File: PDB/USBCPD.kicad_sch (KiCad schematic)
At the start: 43 parts, among them J1 USB_C_Receptacle, Q3 STL6P3LLH6, Q4 STL6P3LLH6, U6 ST1S14PHR, U7 STUSB4700YQTR, U8 STR2P3LLH6, U9 LM76005QRNPRQ1

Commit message: added sd card
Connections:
- net at C22.1, C23.1, C24.1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: now also U7.24 (VDD)
- no-connect marks 14 -> 16
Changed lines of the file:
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@@
-	)
-	(junction
-		(at 353.06 160.02)
-		(diameter 0)
-		(color 0 0 0 0)
 	)
 	(junction
@@
 	)
 	(junction
+		(at 368.3 166.37)
+		(diameter 0)
+		(color 0 0 0 0)
+	)
+	(junction
 		(at 317.5 160.02)
 		(diameter 0)
@@
 	)
 	(junction
+		(at 368.3 160.02)
+		(diameter 0)
+		(color 0 0 0 0)
+	)
+	(junction
 		(at 317.5 162.56)
 		(diameter 0)
@@
 		(diameter 0)
 		(color 0 0 0 0)
+	)
+	(no_connect
+		(at 393.7 223.52)
 	)
 	(no_connect
@@
 	)
 	(no_connect
+		(at 393.7 212.09)
+	)
+	(no_connect
 		(at 480.06 170.18)
 	)
@@
 	(wire
 		(pts
+			(xy 368.3 160.02) (xy 382.27 160.02)
+		)
+		(stroke
+			(width 0)
+			(type default)
+		)
+	)
+	(wire
+		(pts
 			(xy 480.06 218.44) (xy 480.06 219.71)
 		)
@@
 	(wire
 		(pts
-			(xy 353.06 160.02) (xy 353.06 166.37)
+			(xy 368.3 160.02) (xy 368.3 166.37)
 		)
 		(stroke
@@
 	(wire
 		(pts
+			(xy 368.3 179.07) (xy 368.3 166.37)
+		)
+		(stroke
+			(width 0)
+			(type default)
+		)
+	)
+	(wire
+		(pts
 			(xy 229.87 165.1) (xy 229.87 160.02)
 		)
@@
 	(wire
 		(pts
-			(xy 353.06 160.02) (xy 382.27 160.02)
-		)
-		(stroke
-			(width 0)
-			(type default)
-		)
-	)
-	(wire
-		(pts
 			(xy 326.39 234.95) (xy 359.41 234.95)
 		)
@@
 	(wire
 		(pts
-			(xy 330.2 160.02) (xy 353.06 160.02)
+			(xy 330.2 160.02) (xy 368.3 160.02)
 		)
 		(stroke
@@
 		)
 		(stroke
+			(width 0)
+			(type default)
+		)
+	)
+	(wire
+		(pts
+			(xy 368.3 166.37) (xy 353.06 166.37)
+		)
+		(stroke

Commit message: added fuses to each
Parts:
- added F4: TR/3216FF15-R, symbol Device:Fuse
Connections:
- net at C28.1, J1.A4 (VBUS): now also F4.2; no longer Q4.5_8, U7.18 (VBUS_SENSE)
- new net: F4.1, Q4.5_8, U7.18 (VBUS_SENSE)
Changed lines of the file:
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@@
 	)
 	(junction
-		(at 452.12 160.02)
-		(diameter 0)
-		(color 0 0 0 0)
-	)
-	(junction
 		(at 90.17 203.2)
 		(diameter 0)
@@
 	)
 	(junction
+		(at 467.36 160.02)
+		(diameter 0)
+		(color 0 0 0 0)
+	)
+	(junction
 		(at 74.93 154.94)
 		(diameter 0)
@@
 	)
 	(junction
-		(at 467.36 160.02)
-		(diameter 0)
-		(color 0 0 0 0)
-	)
-	(junction
 		(at 364.49 179.07)
 		(diameter 0)
@@
 	)
 	(junction
+		(at 452.12 160.02)
+		(diameter 0)
+		(color 0 0 0 0)
+	)
+	(junction
 		(at 90.17 193.04)
 		(diameter 0)
@@
 	(wire
 		(pts
+			(xy 463.55 160.02) (xy 467.36 160.02)
+		)
+		(stroke
+			(width 0)
+			(type default)
+		)
+	)
+	(wire
+		(pts
 			(xy 306.07 162.56) (xy 317.5 162.56)
 		)
@@
 	(wire
 		(pts
-			(xy 452.12 160.02) (xy 467.36 160.02)
-		)
-		(stroke
-			(width 0)
-			(type default)
-		)
-	)
-	(wire
-		(pts
 			(xy 427.99 180.34) (xy 427.99 194.31)
 		)
@@
 	(wire
 		(pts
+			(xy 452.12 160.02) (xy 455.93 160.02)
+		)
+		(stroke
+			(width 0)
+			(type default)
+		)
+	)
+	(wire
+		(pts
 			(xy 477.52 210.82) (xy 480.06 210.82)
 		)
@@
 					(unit 1)
 				)
+			)
+		)
+	)
+	(symbol
+		(lib_id "Device:Fuse")
+		(at 459.74 160.02 90)
+		(unit 1)
+		(body_style 1)
+		(exclude_from_sim no)
+		(in_bom yes)
+		(on_board yes)
+		(in_pos_files yes)
+		(dnp no)
+		(fields_autoplaced yes)
+		(property "Reference" "F4"
+			(at 459.74 153.67 90)
+			(show_name no)
+			(do_not_autoplace no)
+			(effects
+				(font
+					(size 1.27 1.27)
+				)
+			)
+		)
+		(property "Value" "TR/3216FF15-R"
+			(at 459.74 156.21 90)
+			(show_name no)
+			(do_not_autoplace no)
+			(effects
+				(font
+					(size 1.27 1.27)
+				)
+			)
+		)
+		(property "Footprint" ""
+			(at 459.74 161.798 90)
+			(hide yes)
+			(show_name no)
+			(do_not_autoplace no)
+			(effects
+				(font
+					(size 1.27 1.27)
+				)
+			)
+		)
+		(property "Datasheet" ""
+			(at 459.74 160.02 0)
+			(hide yes)
+			(show_name no)
+			(do_not_autoplace no)
+			(effects
+				(font
+					(size 1.27 1.27)
+				)
+			)
+		)
+		(property "Description" "Fuse"
+			(at 459.74 160.02 0)
+			(hide yes)
+			(show_name no)
+			(do_not_autoplace no)
+			(effects
+				(font
+					(size 1.27 1.27)
+				)
+			)
+		)
+		(pin "2"
+		)
+		(pin "1"
+		)
+		(instances
+			(project "PDB"
+				(path "/a9cf05c4-aac5-4cf1-b700-1d3045f8dfbd/b0911c37-41be-485e-baed-d6c7fecee207"
+					(reference "F4")
+					(unit 1)
+				)

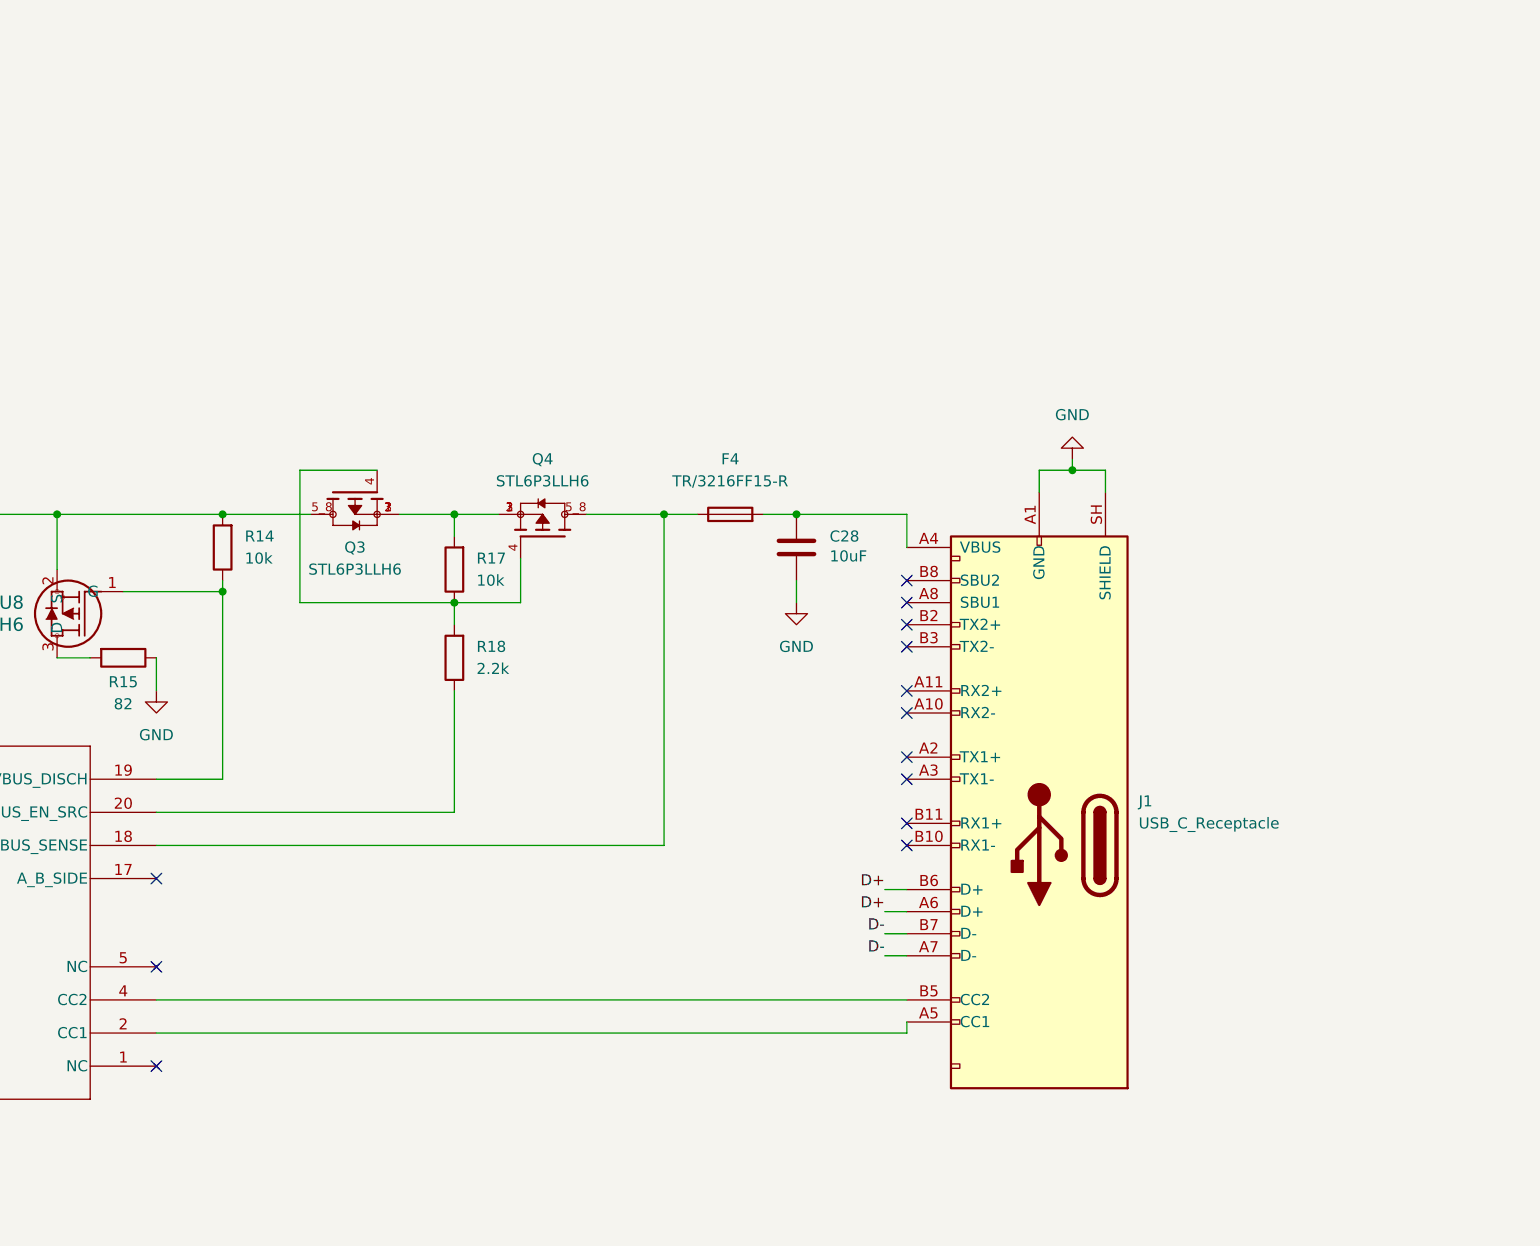
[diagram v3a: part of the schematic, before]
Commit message: added temp sensing on every rail available
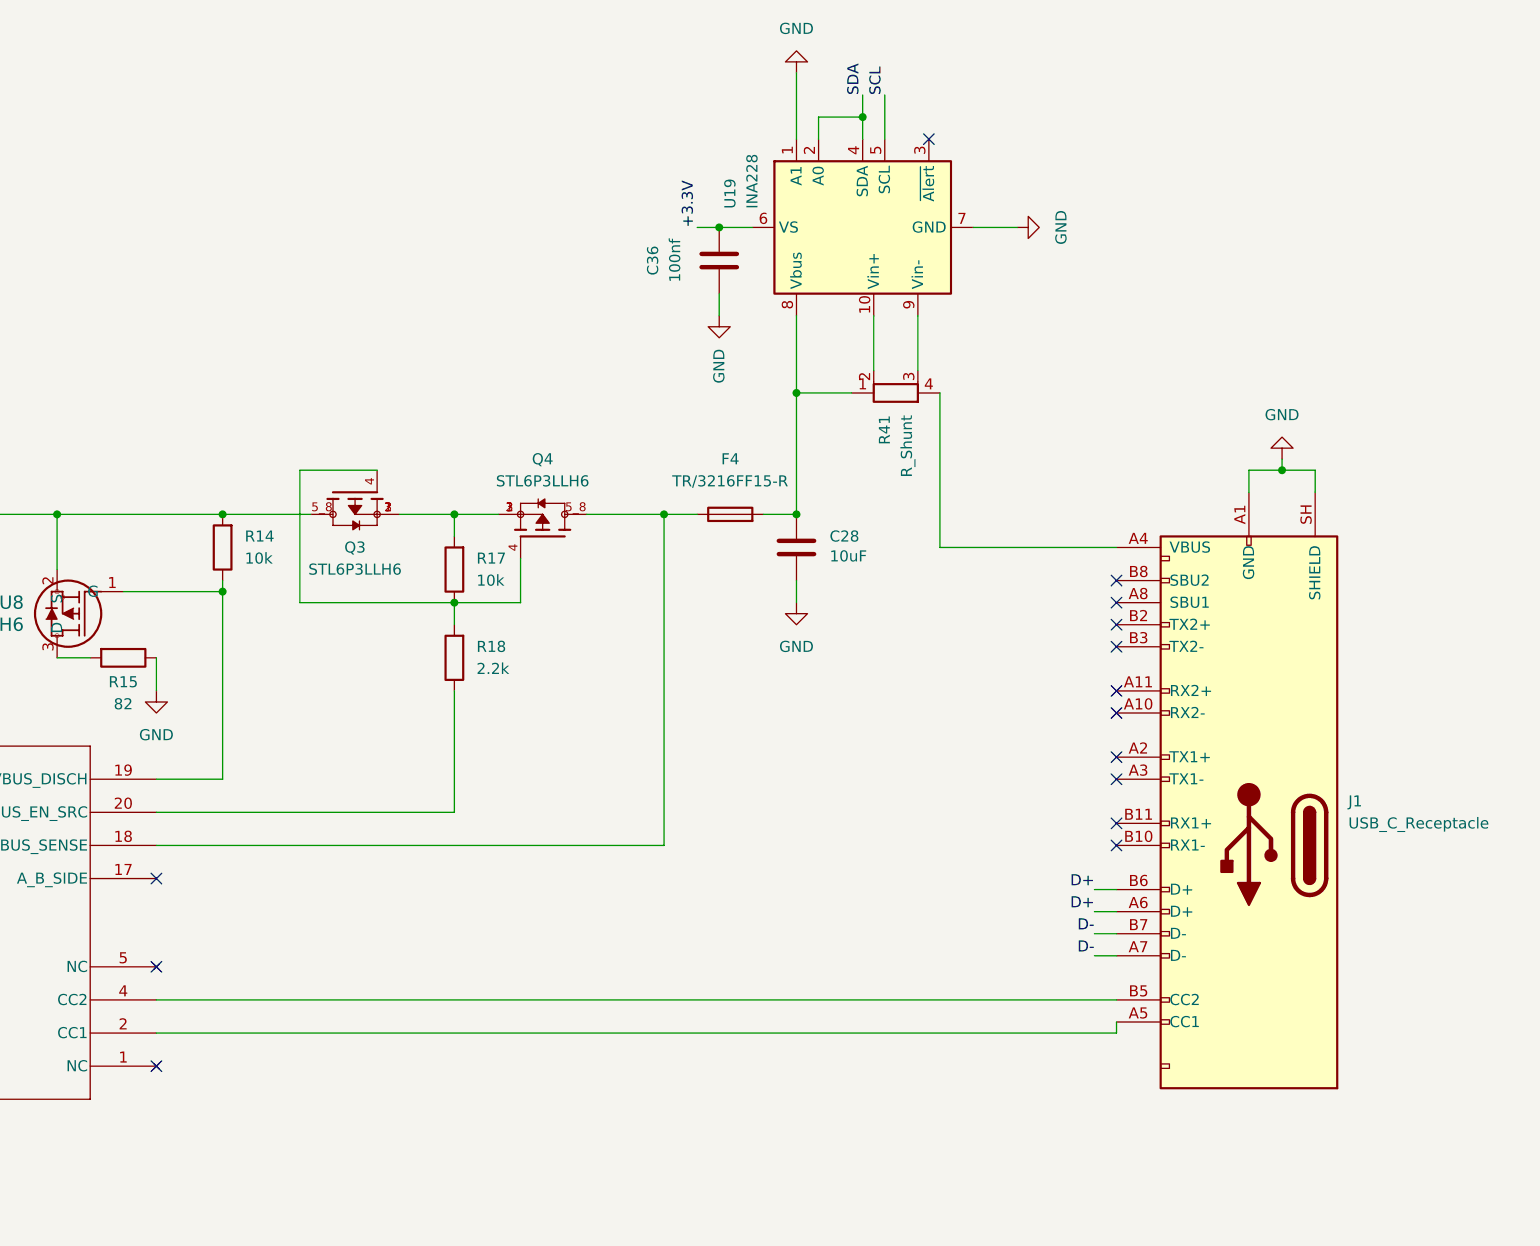
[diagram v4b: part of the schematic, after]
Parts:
- added C36: 100nf, Capacitor_SMD:C_1206_3216Metric, symbol Device:C
- added R41: R_Shunt, symbol Device:R_Shunt
- added U19: INA228, Package_SO:TSSOP-10_3x3mm_P0.5mm, symbol Sensor_Energy:INA228
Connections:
- net GND: now also C36.1, U19.1 (A1), U19.7 (GND)
- net SCL: now also U19.5 (SCL)
- net SDA: now also U19.2 (A0), U19.4 (SDA)
- net at C28.1, F4.2: now also R41.1, U19.8 (Vbus); no longer J1.A4 (VBUS)
- new net: J1.A4 (VBUS), R41.4
- new net: R41.2, U19.10 (Vin+)
- new net: R41.3, U19.9 (Vin-)
- new net +3.3V: C36.2, U19.6 (VS)
- no-connect marks 16 -> 17
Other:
- moved on the sheet: J1

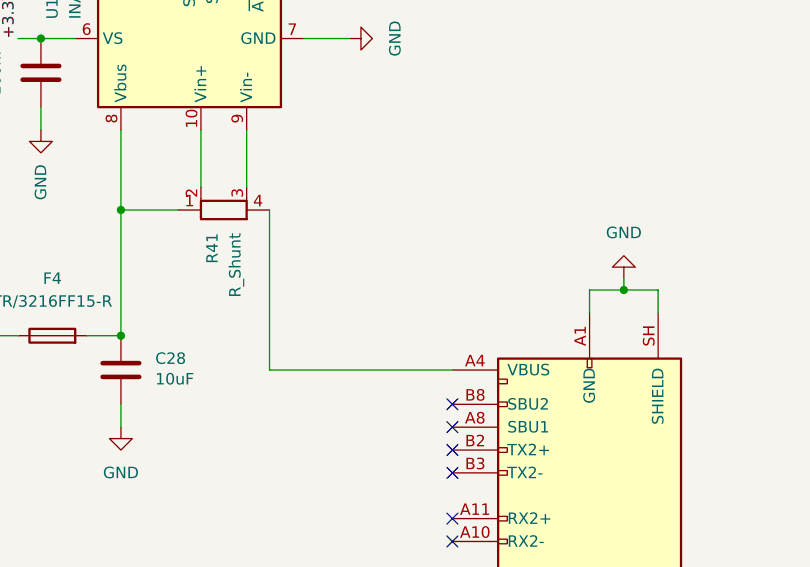
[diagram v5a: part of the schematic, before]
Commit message: added tp's, switches, inputs/outputs
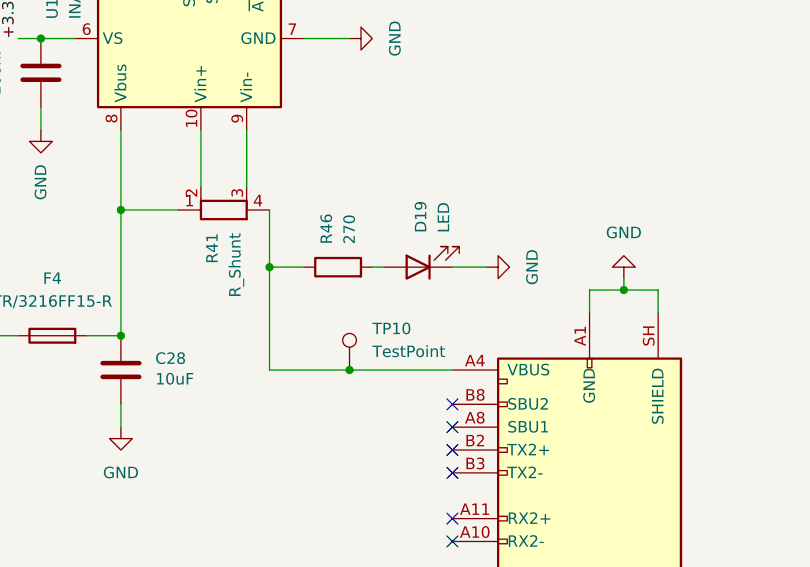
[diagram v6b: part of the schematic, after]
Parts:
- added D19: LED, LED_SMD:LED_0805_2012Metric, symbol Device:LED
- added R46: 270, Resistor_SMD:R_1206_3216Metric_Pad1.30x1.75mm_HandSolder, symbol Device:R
- added TP10: TestPoint, TestPoint:TestPoint_Pad_D2.0mm, symbol Connector:TestPoint
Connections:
- net GND: now also D19.1 (K)
- net at J1.A4 (VBUS), R41.4: now also R46.1, TP10.1
- new net: D19.2 (A), R46.2
